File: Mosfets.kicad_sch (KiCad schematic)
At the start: 29 parts, among them Q1 STB75NF75T4, Q2 STB75NF75T4, Q3 STB75NF75T4, Q4 STB75NF75T4, Q5 STB75NF75T4, Q6 STB75NF75T4

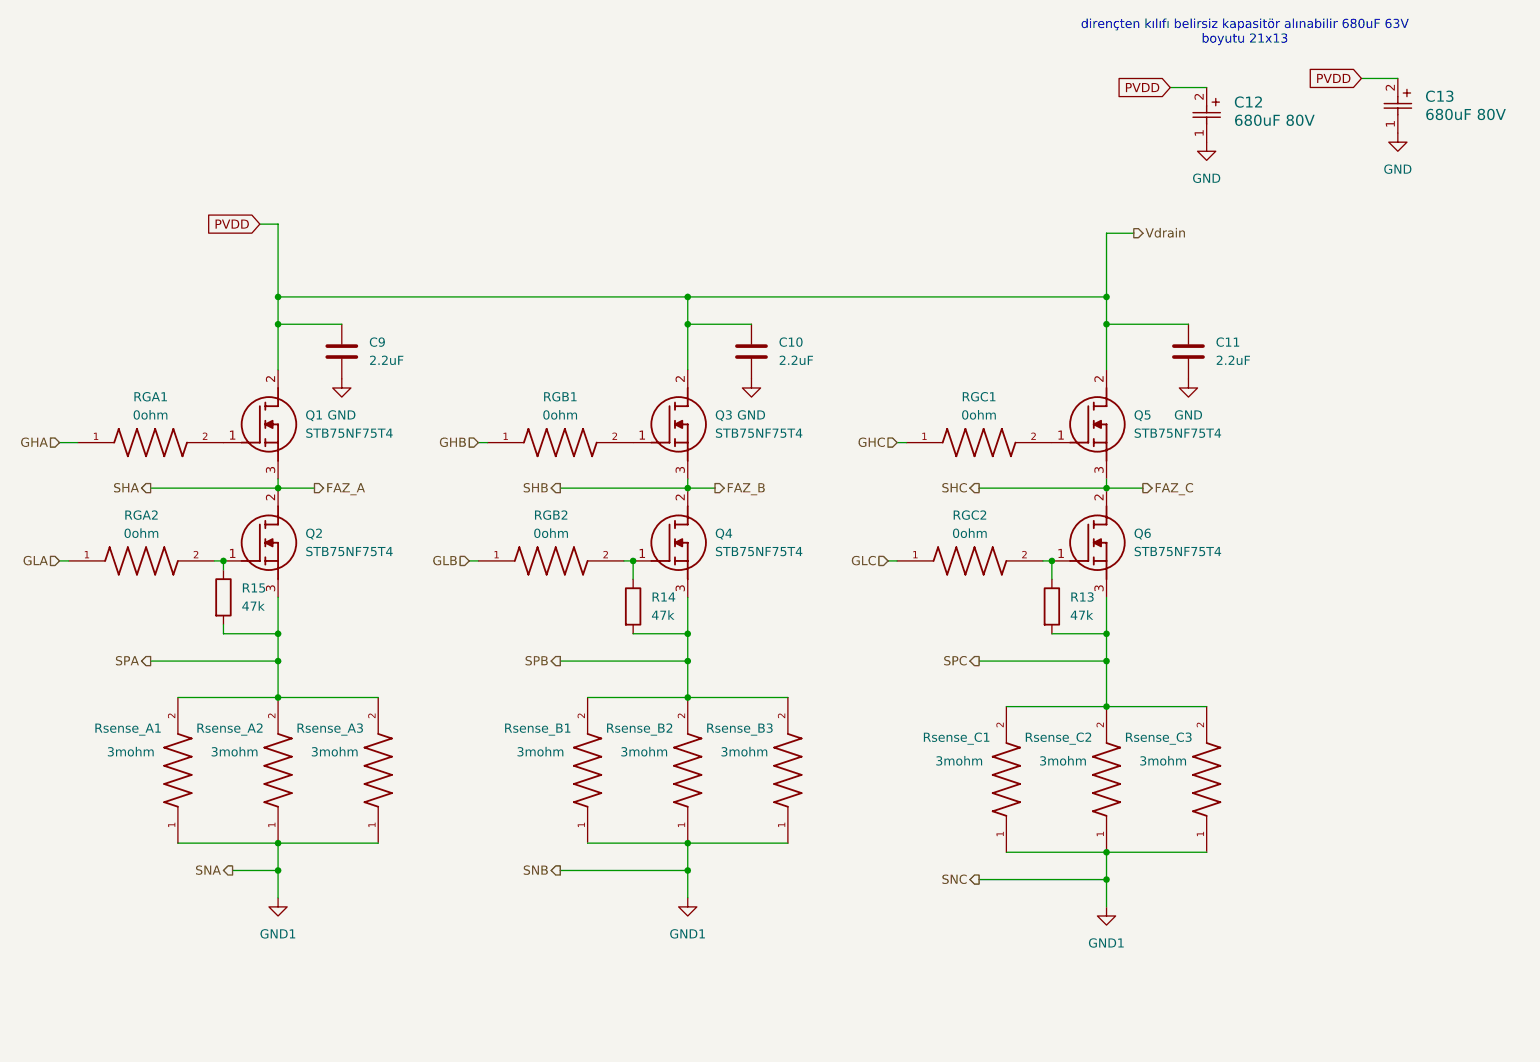
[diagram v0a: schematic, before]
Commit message: Footprints prepared, first pcb project created.
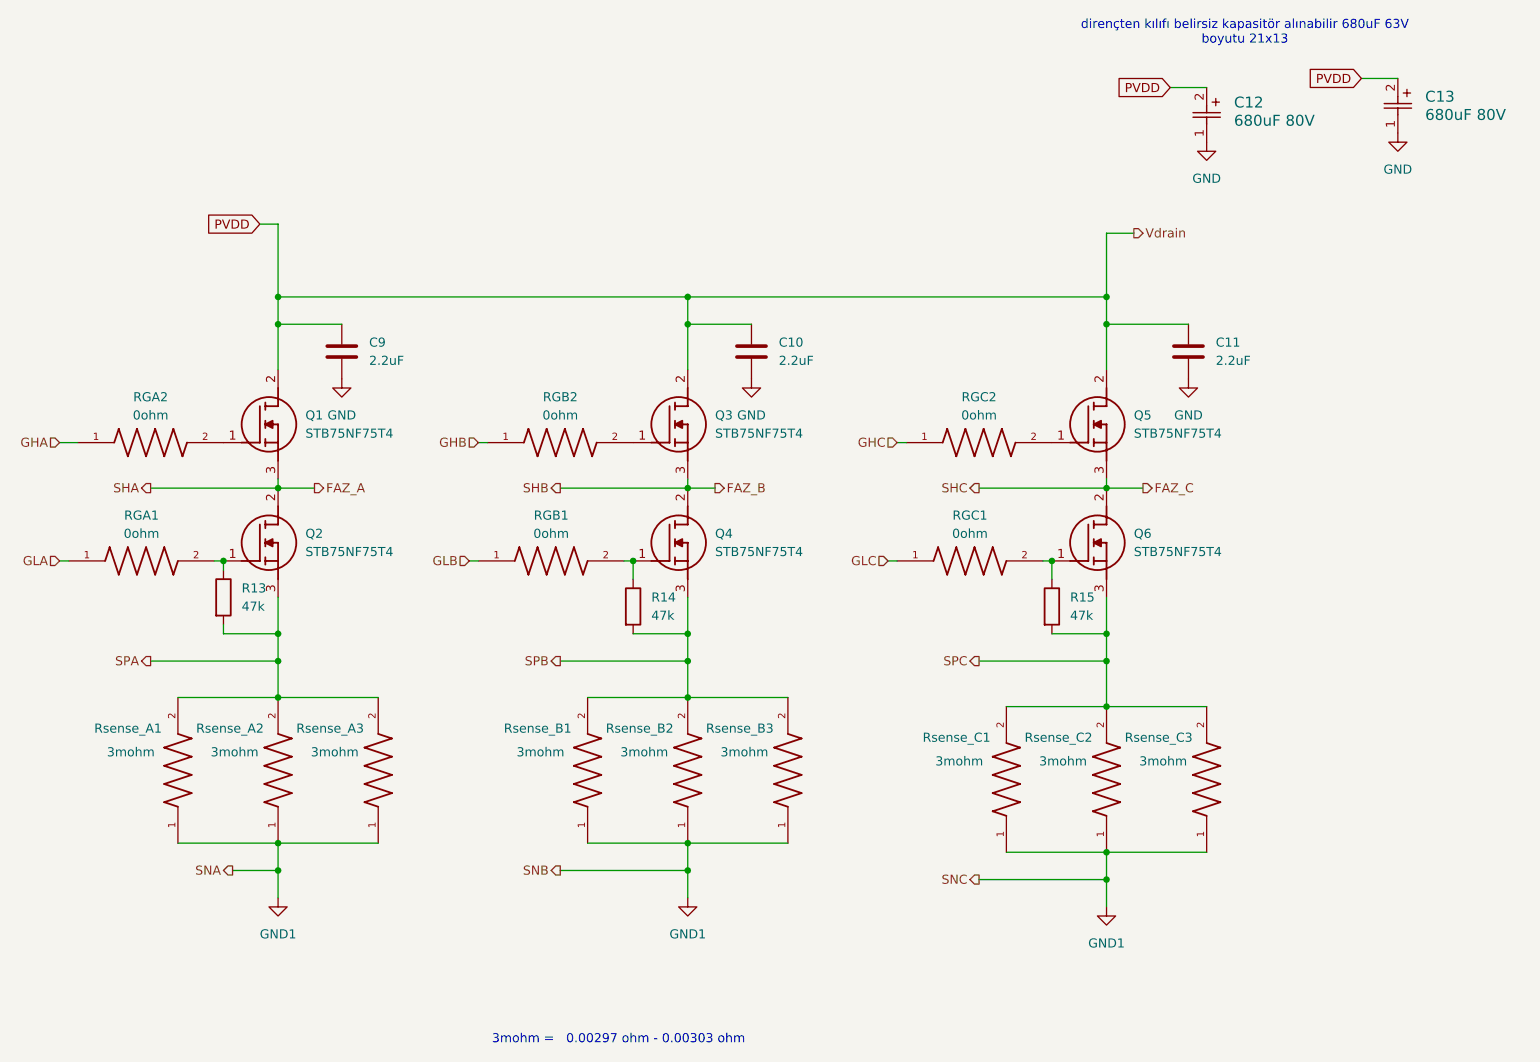
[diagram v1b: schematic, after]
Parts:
- renumbered R15 to R13, R13 to R15, RGA2 to RGA1, RGA1 to RGA2, RGB2 to RGB1, RGB1 to RGB2, RGC2 to RGC1, RGC1 to RGC2
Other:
- note added: "3mohm = 0.00297 ohm - 0.00303 ohm"

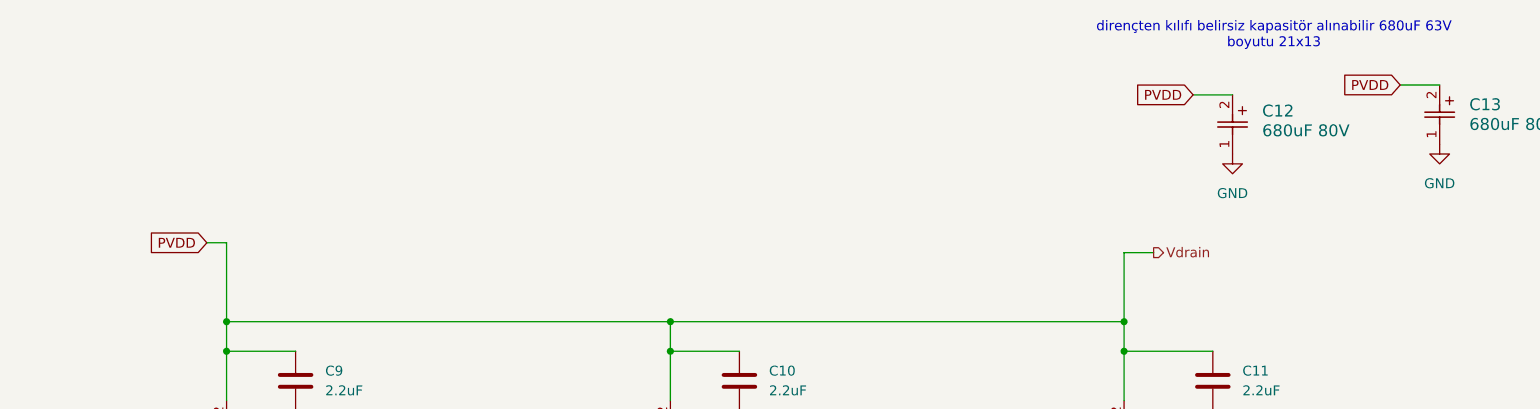
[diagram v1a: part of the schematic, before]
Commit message: some tags chaneged, pcb thinked about pcb component placement, aluminum mosfet carrier pcb and paralelling mosfets
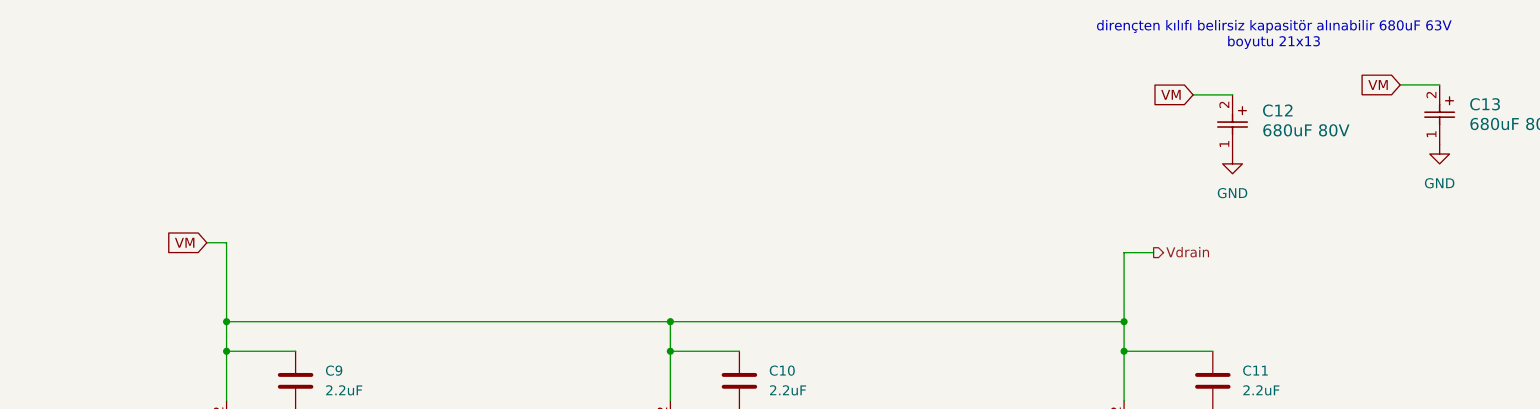
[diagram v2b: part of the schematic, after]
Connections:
- net PVDD renamed VM
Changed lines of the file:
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@@
 		)
 	)
-	(global_label "PVDD"
+	(global_label "VM"
 		(shape input)
 		(at 226.06 29.21 180)
@@
 		)
 	)
-	(global_label "PVDD"
+	(global_label "VM"
 		(shape input)
 		(at 99.06 48.26 180)
@@
 		)
 	)
-	(global_label "PVDD"
+	(global_label "VM"
 		(shape input)
 		(at 252.73 27.94 180)

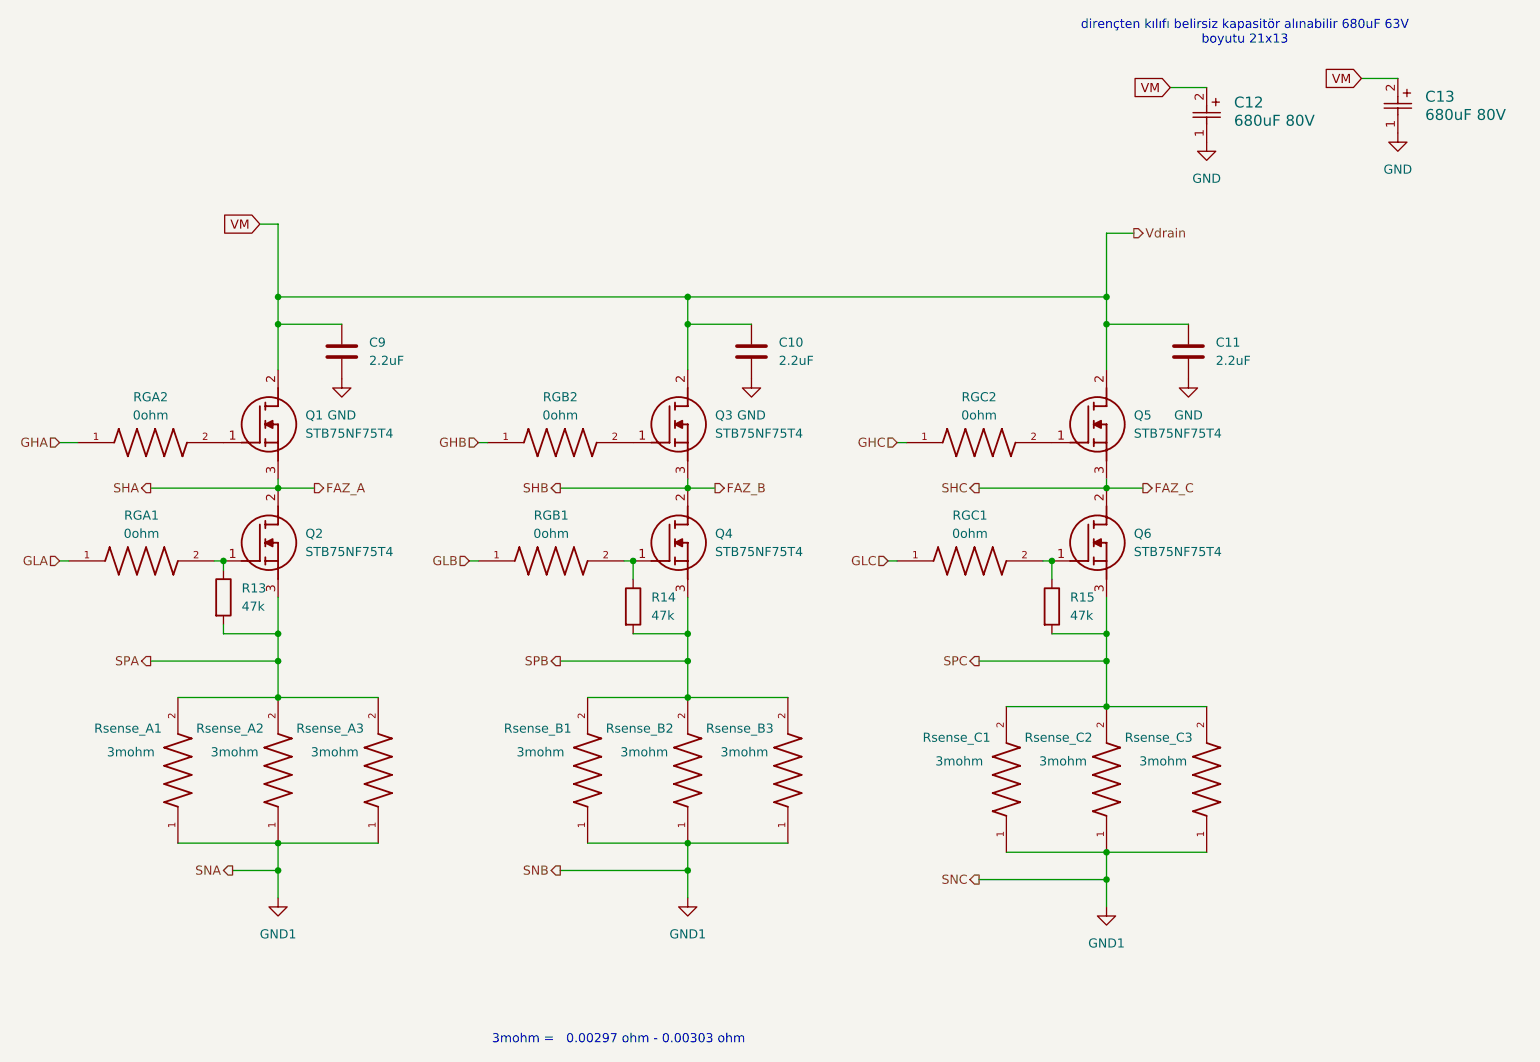
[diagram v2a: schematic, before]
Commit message: New one_GND_Layer pcb desgin has finished yet. DRC Rule checks needs to be controlling and correcting still.
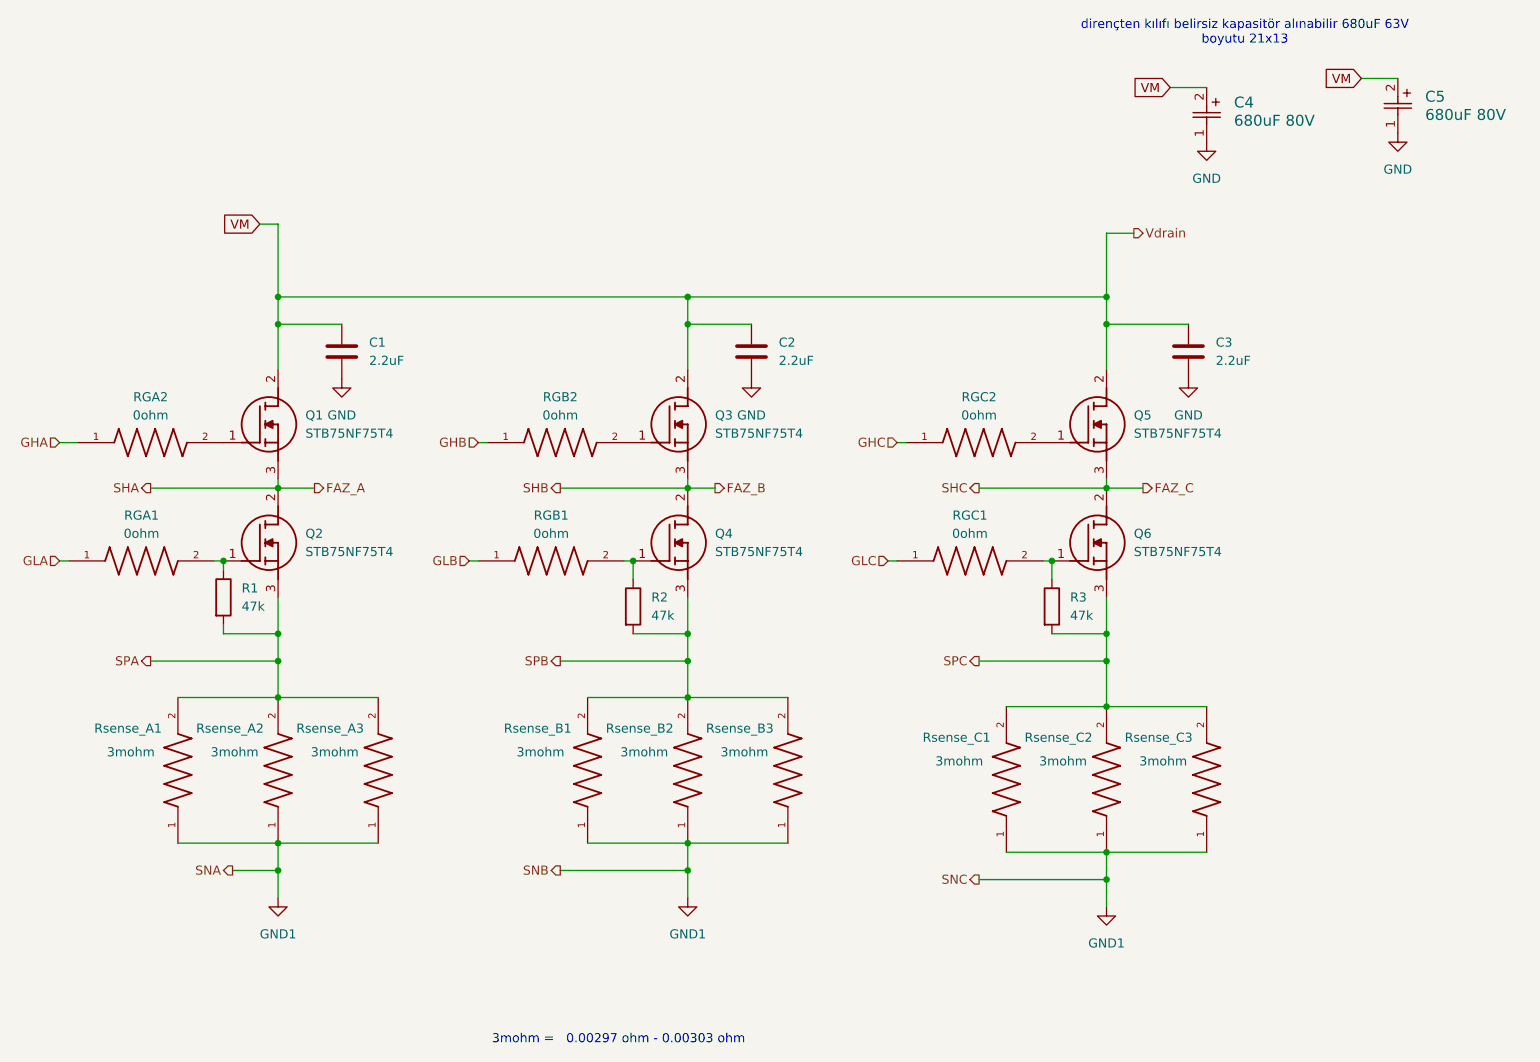
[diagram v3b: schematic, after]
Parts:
- renumbered C9 to C1, C10 to C2, C11 to C3, C12 to C4, C13 to C5, R13 to R1, R14 to R2, R15 to R3
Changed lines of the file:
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@@
 		(dnp no)
 		(fields_autoplaced yes)
-		(property "Reference" "C11"
+		(property "Reference" "C3"
 			(at 232.41 64.7699 0)
 			(effects
@@
 			(project "Ana_ESC"
 				(path "/57129761-6d47-486c-bd7a-90dbb6f75754/93a25273-1af9-476d-be50-92121d872328"
-					(reference "C11")
+					(reference "C3")
 					(unit 1)
 				)
@@
 		(dnp no)
 		(fields_autoplaced yes)
-		(property "Reference" "R14"
+		(property "Reference" "R2"
 			(at 153.67 100.3299 0)
 			(effects
@@
 			(project "Ana_ESC"
 				(path "/57129761-6d47-486c-bd7a-90dbb6f75754/93a25273-1af9-476d-be50-92121d872328"
-					(reference "R14")
+					(reference "R2")
 					(unit 1)
 				)
@@
 		(dnp no)
 		(fields_autoplaced yes)
-		(property "Reference" "#PWR015"
+		(property "Reference" "#PWR07"
 			(at 231.14 43.18 0)
 			(effects
@@
 			(project "Ana_ESC"
 				(path "/57129761-6d47-486c-bd7a-90dbb6f75754/93a25273-1af9-476d-be50-92121d872328"
-					(reference "#PWR015")
+					(reference "#PWR07")
 					(unit 1)
 				)
@@
 		(dnp no)
 		(fields_autoplaced yes)
-		(property "Reference" "C12"
+		(property "Reference" "C4"
 			(at 234.95 31.2927 90)
 			(effects
@@
 			(project "Ana_ESC"
 				(path "/57129761-6d47-486c-bd7a-90dbb6f75754/93a25273-1af9-476d-be50-92121d872328"
-					(reference "C12")
+					(reference "C4")
 					(unit 1)
 				)
@@
 		(dnp no)
 		(fields_autoplaced yes)
-		(property "Reference" "#PWR012"
+		(property "Reference" "#PWR04"
 			(at 167.64 76.2 0)
 			(effects
@@
 			(project "Ana_ESC"
 				(path "/57129761-6d47-486c-bd7a-90dbb6f75754/93a25273-1af9-476d-be50-92121d872328"
-					(reference "#PWR012")
+					(reference "#PWR04")
 					(unit 1)
 				)
@@
 		(dnp no)
 		(fields_autoplaced yes)
-		(property "Reference" "R13"
+		(property "Reference" "R1"
 			(at 96.52 99.0599 0)
 			(effects
@@
 			(project "Ana_ESC"
 				(path "/57129761-6d47-486c-bd7a-90dbb6f75754/93a25273-1af9-476d-be50-92121d872328"
-					(reference "R13")
+					(reference "R1")
 					(unit 1)
 				)
@@
 		(dnp no)
 		(fields_autoplaced yes)
-		(property "Reference" "C13"
+		(property "Reference" "C5"
 			(at 261.62 30.4799 90)
 			(effects
@@
 			(project "Ana_ESC"
 				(path "/57129761-6d47-486c-bd7a-90dbb6f75754/93a25273-1af9-476d-be50-92121d872328"
-					(reference "C13")
+					(reference "C5")
 					(unit 1)
 				)
@@
 		(dnp no)
 		(fields_autoplaced yes)
-		(property "Reference" "C9"
+		(property "Reference" "C1"
 			(at 114.3 64.7699 0)
 			(effects
@@
 			(project "Ana_ESC"
 				(path "/57129761-6d47-486c-bd7a-90dbb6f75754/93a25273-1af9-476d-be50-92121d872328"
-					(reference "C9")
+					(reference "C1")
 					(unit 1)
 				)
@@
 		(dnp no)
 		(fields_autoplaced yes)
-		(property "Reference" "C10"
+		(property "Reference" "C2"
 			(at 171.45 64.7699 0)
 			(effects
@@
 			(project "Ana_ESC"
 				(path "/57129761-6d47-486c-bd7a-90dbb6f75754/93a25273-1af9-476d-be50-92121d872328"
-					(reference "C10")
+					(reference "C2")
 					(unit 1)
 				)
@@
 		(dnp no)
 		(fields_autoplaced yes)
-		(property "Reference" "#PWR014"
+		(property "Reference" "#PWR06"
 			(at 228.6 76.2 0)
 			(effects
@@
 			(project "Ana_ESC"
 				(path "/57129761-6d47-486c-bd7a-90dbb6f75754/93a25273-1af9-476d-be50-92121d872328"
-					(reference "#PWR014")
+					(reference "#PWR06")
 					(unit 1)
 				)
@@
 		(dnp no)
 		(fields_autoplaced yes)
-		(property "Reference" "#PWR016"
+		(property "Reference" "#PWR08"
 			(at 257.81 41.91 0)
 			(effects
@@
 			(project "Ana_ESC"
 				(path "/57129761-6d47-486c-bd7a-90dbb6f75754/93a25273-1af9-476d-be50-92121d872328"
-					(reference "#PWR016")
+					(reference "#PWR08")
 					(unit 1)
 				)
@@
 		(dnp no)
 		(fields_autoplaced yes)
-		(property "Reference" "R15"
+		(property "Reference" "R3"
 			(at 212.09 100.3299 0)
 			(effects
@@
 			(project "Ana_ESC"
 				(path "/57129761-6d47-486c-bd7a-90dbb6f75754/93a25273-1af9-476d-be50-92121d872328"
-					(reference "R15")
+					(reference "R3")
 					(unit 1)
 				)
@@
 		(dnp no)
 		(fields_autoplaced yes)
-		(property "Reference" "#PWR013"
+		(property "Reference" "#PWR05"
 			(at 217.17 149.86 0)
 			(effects
@@
 			(project "Ana_ESC"
 				(path "/57129761-6d47-486c-bd7a-90dbb6f75754/93a25273-1af9-476d-be50-92121d872328"
-					(reference "#PWR013")
+					(reference "#PWR05")
 					(unit 1)
 				)
